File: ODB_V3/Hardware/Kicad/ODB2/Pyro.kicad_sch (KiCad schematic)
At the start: 51 parts, among them J1 Screw_Terminal_01x08, U11 SI5442DU-T1-GE3, U12 SI5442DU-T1-GE3, U2 LM339, U3 SI5442DU-T1-GE3, U8 SI5442DU-T1-GE3

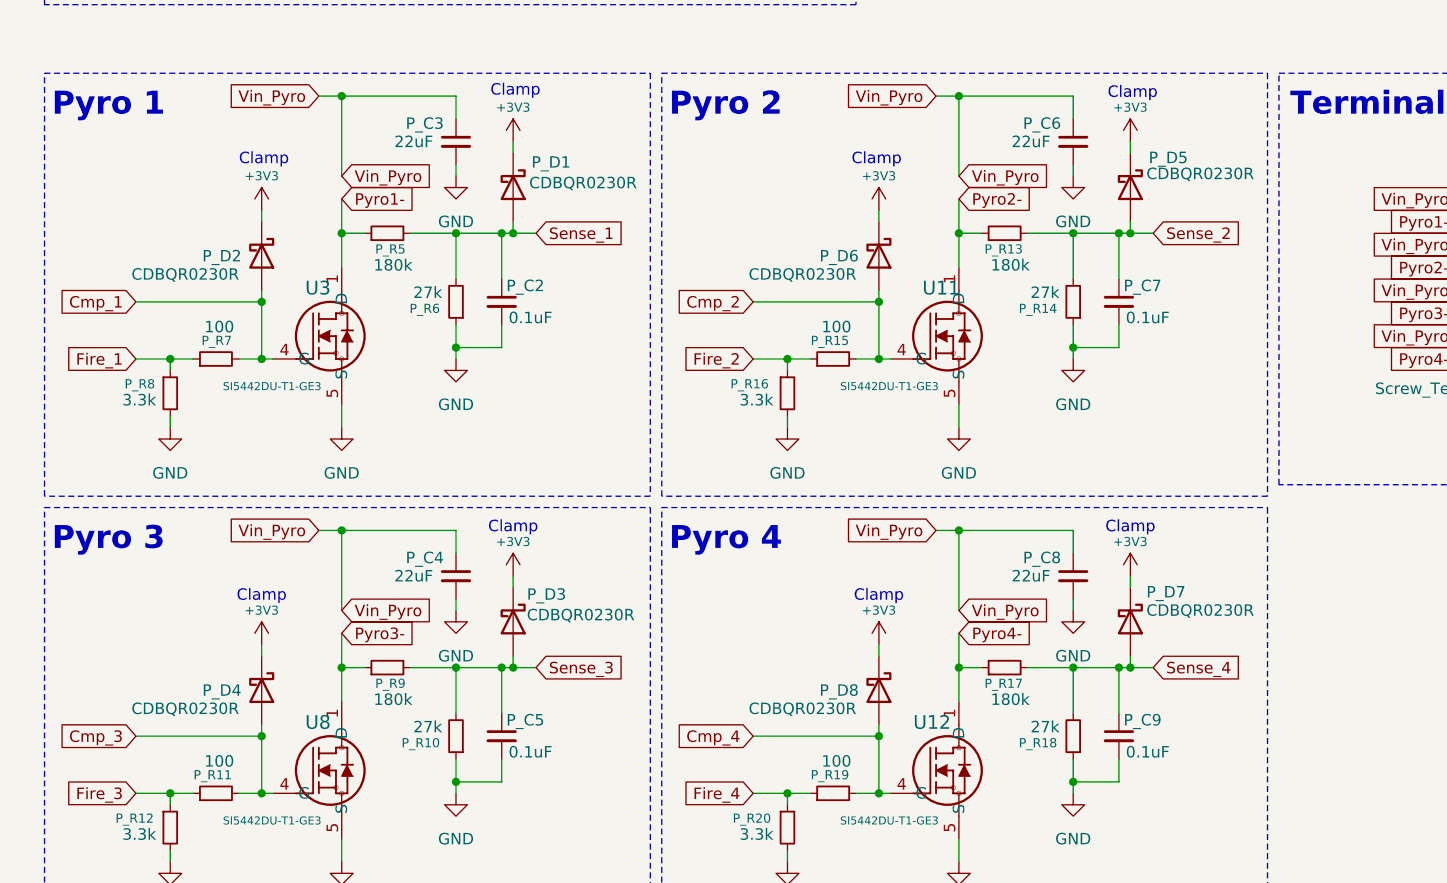
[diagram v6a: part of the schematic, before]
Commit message: wip : digikey part number et lien pour toutes pièces importantes (pas résistances, capacités, etc)
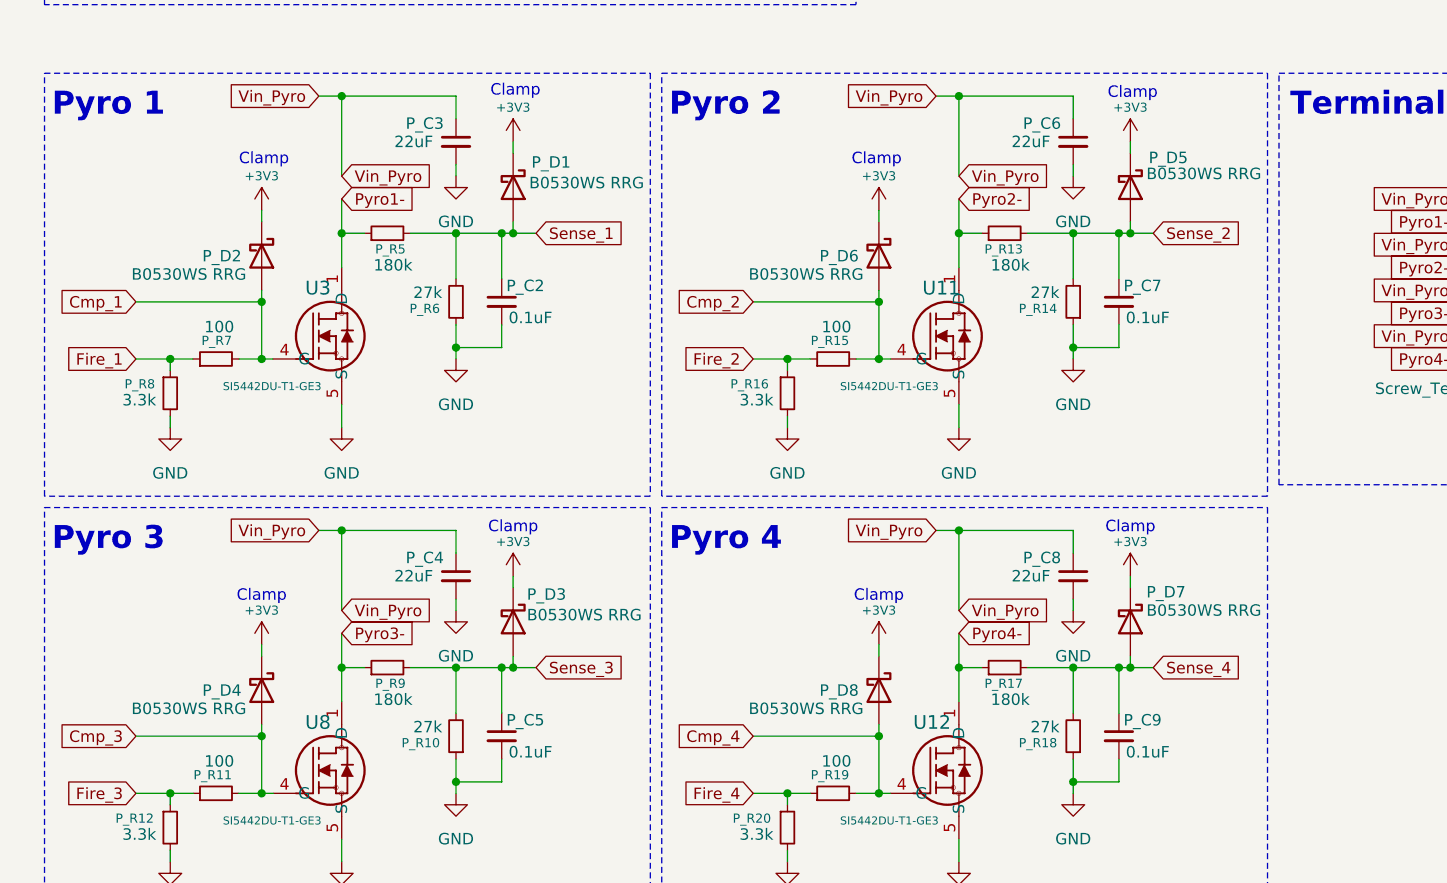
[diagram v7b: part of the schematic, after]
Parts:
- J1: DigiKey_Part_Number (none) -> 277-1279-ND
- PA_Q1: DigiKey_Part_Number (none) -> MMBT3904LT1GOSCT-ND; Digikey (none) -> MMBT3904LT1GOSCT-ND
- PA_Q3: DigiKey_Part_Number (none) -> SI7617DN-T1-GE3CT-ND
- P_D1, P_D2, P_D3, P_D4, P_D5, P_D6, P_D7, P_D8: value CDBQR0230R -> B0530WS RRG; DigiKey_Part_Number (none) -> B0530WSRRGCT-ND
- U11, U12, U3, U8: DigiKey_Part_Number (none) -> SI5442DU-T1-GE3CT-ND
- U2: DigiKey_Part_Number (none) -> 296-1013-1-ND; Purchase-URL (none) -> https://www.digikey.ca/en/products/detail/texas-instruments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
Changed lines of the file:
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@@
 			)
 		)
-		(property "Datasheet" "https://www.vishay.com/doc?63233"
+		(property "Datasheet" "https://www.digikey.com/en/products/detail/vishay-siliconix/SI5442DU-T1-GE3/4142130"
 			(at 109.22 177.8 0)
 			(effects
@@
 			)
 		)
-		(property "DigiKey_Part_Number" ""
+		(property "DigiKey_Part_Number" "SI5442DU-T1-GE3CT-ND"
 			(at 109.22 177.8 0)
 			(effects
@@
 			)
 		)
-		(property "Value" "CDBQR0230R"
+		(property "Value" "B0530WS RRG"
 			(at 69.088 109.982 90)
 			(effects
@@
 			)
 		)
-		(property "Datasheet" "https://assets.nexperia.com/documents/data-sheet/BAT54J.pdf"
+		(property "Datasheet" "https://www.digikey.ca/en/products/detail/taiwan-semiconductor-corporation/B0530WS-RRG/7357154"
 			(at 67.31 110.49 0)
 			(effects
@@
 			)
 		)
-		(property "DigiKey_Part_Number" ""
+		(property "DigiKey_Part_Number" "B0530WSRRGCT-ND"
 			(at 67.31 110.49 90)
 			(effects
@@
 			)
 		)
-		(property "DigiKey_Part_Number" ""
+		(property "DigiKey_Part_Number" "296-1013-1-ND"
 			(at 58.42 46.99 0)
 			(effects
@@
 			)
 		)
-		(property "Purchase-URL" ""
+		(property "Purchase-URL" "https://www.digikey.ca/en/products/detail/texas-instruments/LM339DR/276657"
 			(at 58.42 46.99 0)
 			(effects
@@
 			)
 		)
-		(property "Value" "CDBQR0230R"
+		(property "Value" "B0530WS RRG"
 			(at 68.834 157.988 90)
 			(effects
@@
 			)
 		)
-		(property "Datasheet" "https://assets.nexperia.com/documents/data-sheet/BAT54J.pdf"
+		(property "Datasheet" "https://www.digikey.ca/en/products/detail/taiwan-semiconductor-corporation/B0530WS-RRG/7357154"
 			(at 67.31 158.75 0)
 			(effects
@@
 			)
 		)
-		(property "DigiKey_Part_Number" ""
+		(property "DigiKey_Part_Number" "B0530WSRRGCT-ND"
 			(at 67.31 158.75 90)
 			(effects
@@
 			)
 		)
-		(property "DigiKey_Part_Number" ""
+		(property "DigiKey_Part_Number" "296-1013-1-ND"
 			(at 58.42 72.39 0)
 			(effects
@@
 			)
 		)
-		(property "Purchase-URL" ""
+		(property "Purchase-URL" "https://www.digikey.ca/en/products/detail/texas-instruments/LM339DR/276657"
 			(at 58.42 72.39 0)
 			(effects
@@
 			)
 		)
-		(property "Value" "CDBQR0230R"
+		(property "Value" "B0530WS RRG"
 			(at 24.892 120.142 90)
 			(effects
@@
 			)
 		)
-		(property "Datasheet" "https://assets.nexperia.com/documents/data-sheet/BAT54J.pdf"
+		(property "Datasheet" "https://www.digikey.ca/en/products/detail/taiwan-semiconductor-corporation/B0530WS-RRG/7357154"
 			(at 39.37 118.11 0)
 			(effects
@@
 			)
 		)
-		(property "DigiKey_Part_Number" ""
+		(property "DigiKey_Part_Number" "B0530WSRRGCT-ND"
 			(at 39.37 118.11 90)
 			(effects
@@
 			)
 		)
-		(property "Value" "CDBQR0230R"
+		(property "Value" "B0530WS RRG"
 			(at 24.892 168.402 90)
 			(effects
@@
 			)
 		)
-		(property "Datasheet" "https://assets.nexperia.com/documents/data-sheet/BAT54J.pdf"
+		(property "Datasheet" "https://www.digikey.ca/en/products/detail/taiwan-semiconductor-corporation/B0530WS-RRG/7357154"
 			(at 39.37 166.37 0)
 			(effects
@@
 			)
 		)
-		(property "DigiKey_Part_Number" ""
+		(property "DigiKey_Part_Number" "B0530WSRRGCT-ND"
 			(at 39.37 166.37 90)
 			(effects
@@
 			)
 		)
-		(property "DigiKey_Part_Number" ""
+		(property "DigiKey_Part_Number" "296-1013-1-ND"
 			(at 58.42 34.29 0)
 			(effects
@@
 			)
 		)
-		(property "Purchase-URL" ""
+		(property "Purchase-URL" "https://www.digikey.ca/en/products/detail/texas-instruments/LM339DR/276657"
 			(at 58.42 34.29 0)
 			(effects
@@
 			)
 		)
-		(property "Datasheet" "https://www.onsemi.com/pdf/datasheet/pzt3904-d.pdf"
+		(property "Datasheet" "https://www.digikey.ca/en/products/detail/onsemi/MMBT3904LT1G/1139813"
 			(at 215.9 49.53 0)
 			(effects
@@
 			)
 		)
-		(property "DigiKey_Part_Number" ""
+		(property "DigiKey_Part_Number" "MMBT3904LT1GOSCT-ND"
 			(at 215.9 49.53 0)
 			(effects
@@
 			)
 		)
+		(property "Digikey" "MMBT3904LT1GOSCT-ND"
+			(at 215.9 49.53 0)
+			(effects
+				(font
+					(size 1.27 1.27)
+				)
+				(hide yes)
+			)
+		)
 		(pin "1"
 		)
@@
 			)
 		)
-		(property "Datasheet" "https://www.vishay.com/doc?63233"
+		(property "Datasheet" "https://www.digikey.com/en/products/detail/vishay-siliconix/SI5442DU-T1-GE3/4142130"
 			(at 109.22 129.54 0)
 			(effects
@@
 			)
 		)
-		(property "DigiKey_Part_Number" ""
+		(property "DigiKey_Part_Number" "SI5442DU-T1-GE3CT-ND"
 			(at 109.22 129.54 0)
 			(effects
@@
 			)
 		)
-		(property "Datasheet" "https://www.vishay.com/doc?65164"
+		(property "Datasheet" "https://www.digikey.ca/en/products/detail/vishay-siliconix/SI7617DN-T1-GE3/2441735"
 			(at 226.06 33.02 0)
 			(effects
@@
 			)
 		)
-		(property "DigiKey_Part_Number" ""
+		(property "DigiKey_Part_Number" "SI7617DN-T1-GE3CT-ND"
 			(at 226.06 33.02 0)
 			(effects
@@
 			)
 		)
-		(property "DigiKey_Part_Number" ""
+		(property "DigiKey_Part_Number" "296-1013-1-ND"
 			(at 90.17 53.34 0)
 			(effects
@@
 			)
 		)
-		(property "Purchase-URL" ""
+		(property "Purchase-URL" "https://www.digikey.ca/en/products/detail/texas-instruments/LM339DR/276657"
 			(at 90.17 53.34 0)
 			(effects
@@
 			)
 		)
-		(property "Datasheet" "~"
+		(property "Datasheet" "https://www.digikey.ca/en/products/detail/phoenix-contact/1725711/267468?gclsrc=aw.ds&gad_source=1&gad_campaignid=20539025167&gbraid=0AAAAADrbLli7yMF8AWC3OGDeDtnxtbfT4&gclid=CjwKCAiAmePKBhAfEiwAU3Ko3HDFvolF9BsdpkRYg5j-UTxoh0sbjQ5grqNJHSHlJ0Sb2VUXdgPsrBoCaTUQAvD_BwE"
 			(at 181.61 119.38 0)
 			(effects
@@
 			)
 		)
-		(property "DigiKey_Part_Number" ""
+		(property "DigiKey_Part_Number" "277-1279-ND"
 			(at 181.61 119.38 0)
 			(effects
@@
 			)
 		)
-		(property "Datasheet" "https://www.vishay.com/doc?63233"
+		(property "Datasheet" "https://www.digikey.com/en/products/detail/vishay-siliconix/SI5442DU-T1-GE3/4142130"
 			(at 40.64 177.8 0)
 			(effects
@@
 			)
 		)
-		(property "DigiKey_Part_Number" ""
+		(property "DigiKey_Part_Number" "SI5442DU-T1-GE3CT-ND"
 			(at 40.64 177.8 0)
 			(effects
@@
 			)
 		)
-		(property "Datasheet" "https://www.vishay.com/doc?63233"
+		(property "Datasheet" "https://www.digikey.com/en/products/detail/vishay-siliconix/SI5442DU-T1-GE3/4142130"
 			(at 40.64 129.54 0)
 			(effects
@@
 			)
 		)
-		(property "DigiKey_Part_Number" ""
+		(property "DigiKey_Part_Number" "SI5442DU-T1-GE3CT-ND"
 			(at 40.64 129.54 0)
 			(effects
@@
 			)
 		)
-		(property "DigiKey_Part_Number" ""
+		(property "DigiKey_Part_Number" "296-1013-1-ND"
 			(at 58.42 59.69 0)
 			(effects
@@
 			)
 		)
-		(property "Purchase-URL" ""
+		(property "Purchase-URL" "https://www.digikey.ca/en/products/detail/texas-instruments/LM339DR/276657"
 			(at 58.42 59.69 0)
 			(effects
@@
 			)
 		)
-		(property "Value" "CDBQR0230R"
+		(property "Value" "B0530WS RRG"
 			(at 93.472 120.142 90)
 			(effects
@@
 			)
 		)
-		(property "Datasheet" "https://assets.nexperia.com/documents/data-sheet/BAT54J.pdf"
+		(property "Datasheet" "https://www.digikey.ca/en/products/detail/taiwan-semiconductor-corporation/B0530WS-RRG/7357154"
 			(at 107.95 118.11 0)
 			(effects
@@
 			)
 		)
-		(property "DigiKey_Part_Number" ""
+		(property "DigiKey_Part_Number" "B0530WSRRGCT-ND"
 			(at 107.95 118.11 90)
 			(effects
@@
 			)
 		)
-		(property "Value" "CDBQR0230R"
+		(property "Value" "B0530WS RRG"
 			(at 137.668 157.48 90)
 			(effects
@@
 			)
 		)
-		(property "Datasheet" "https://assets.nexperia.com/documents/data-sheet/BAT54J.pdf"
+		(property "Datasheet" "https://www.digikey.ca/en/products/detail/taiwan-semiconductor-corporation/B0530WS-RRG/7357154"
 			(at 135.89 158.75 0)
 			(effects
@@
 			)
 		)
-		(property "DigiKey_Part_Number" ""
+		(property "DigiKey_Part_Number" "B0530WSRRGCT-ND"
 			(at 135.89 158.75 90)
 			(effects
@@
 			)
 		)
-		(property "Value" "CDBQR0230R"
+		(property "Value" "B0530WS RRG"
 			(at 137.668 108.966 90)
 			(effects
@@
 			)
 		)
-		(property "Datasheet" "https://assets.nexperia.com/documents/data-sheet/BAT54J.pdf"
+		(property "Datasheet" "https://www.digikey.ca/en/products/detail/taiwan-semiconductor-corporation/B0530WS-RRG/7357154"
 			(at 135.89 110.49 0)
 			(effects
@@
 			)
 		)
-		(property "DigiKey_Part_Number" ""
+		(property "DigiKey_Part_Number" "B0530WSRRGCT-ND"
 			(at 135.89 110.49 90)
 			(effects
@@
 			)
 		)
-		(property "Value" "CDBQR0230R"
+		(property "Value" "B0530WS RRG"
 			(at 93.472 168.402 90)
 			(effects
@@
 			)
 		)
-		(property "Datasheet" "https://assets.nexperia.com/documents/data-sheet/BAT54J.pdf"
+		(property "Datasheet" "https://www.digikey.ca/en/products/detail/taiwan-semiconductor-corporation/B0530WS-RRG/7357154"
 			(at 107.95 166.37 0)
 			(effects
@@
 			)
 		)
-		(property "DigiKey_Part_Number" ""
+		(property "DigiKey_Part_Number" "B0530WSRRGCT-ND"
 			(at 107.95 166.37 90)
 			(effects

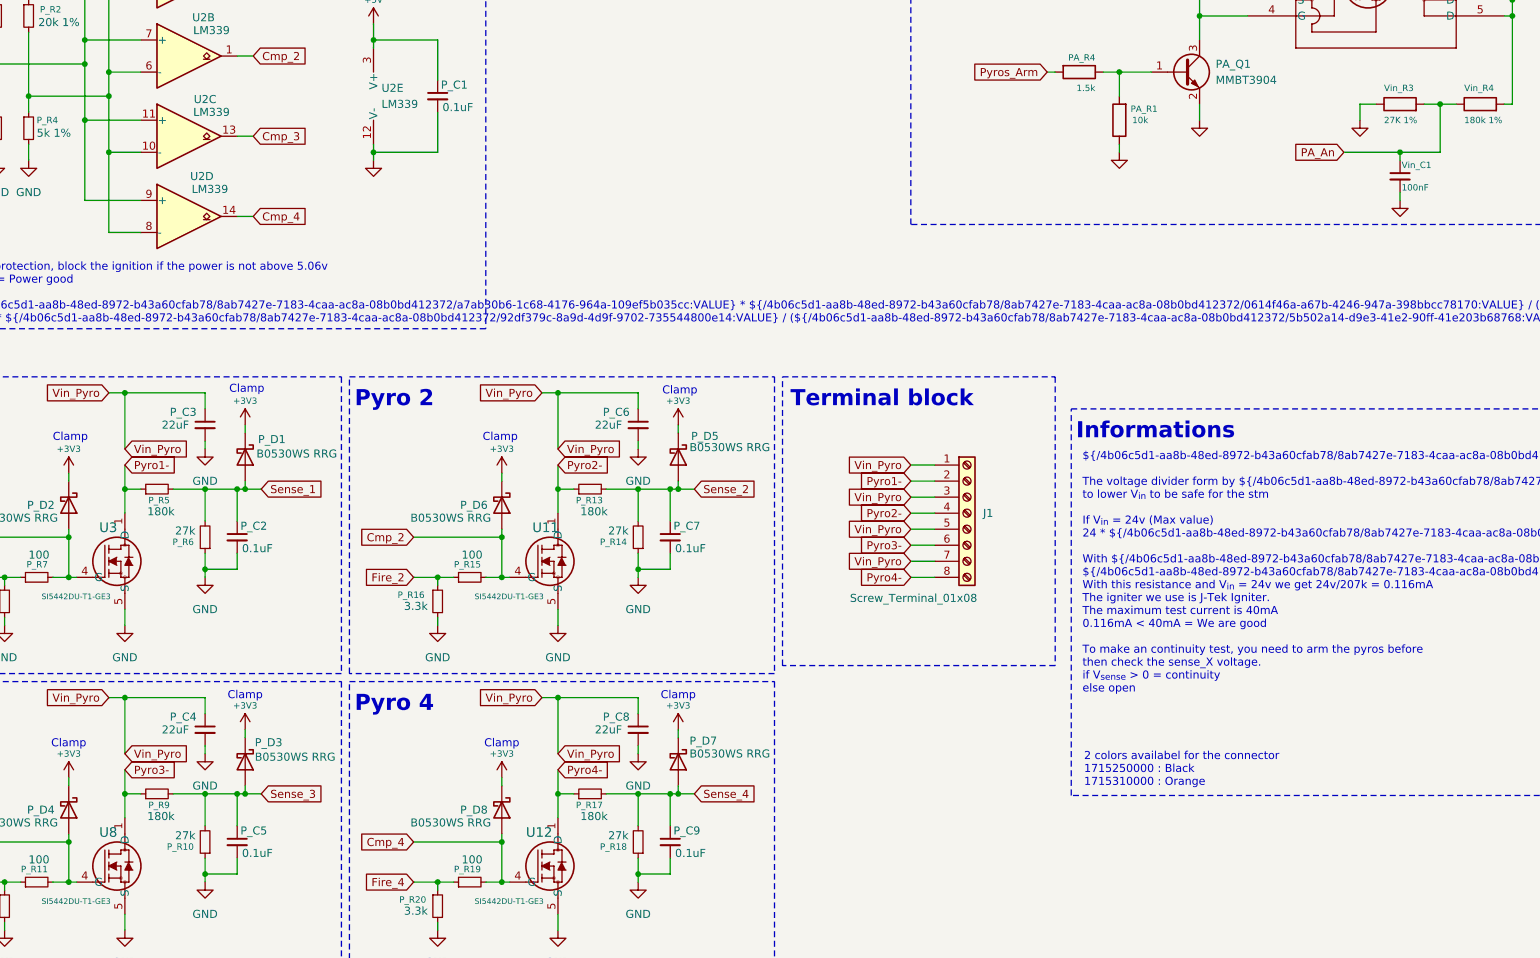
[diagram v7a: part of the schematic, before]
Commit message: fix : change pieces and footprints to reduce BOM
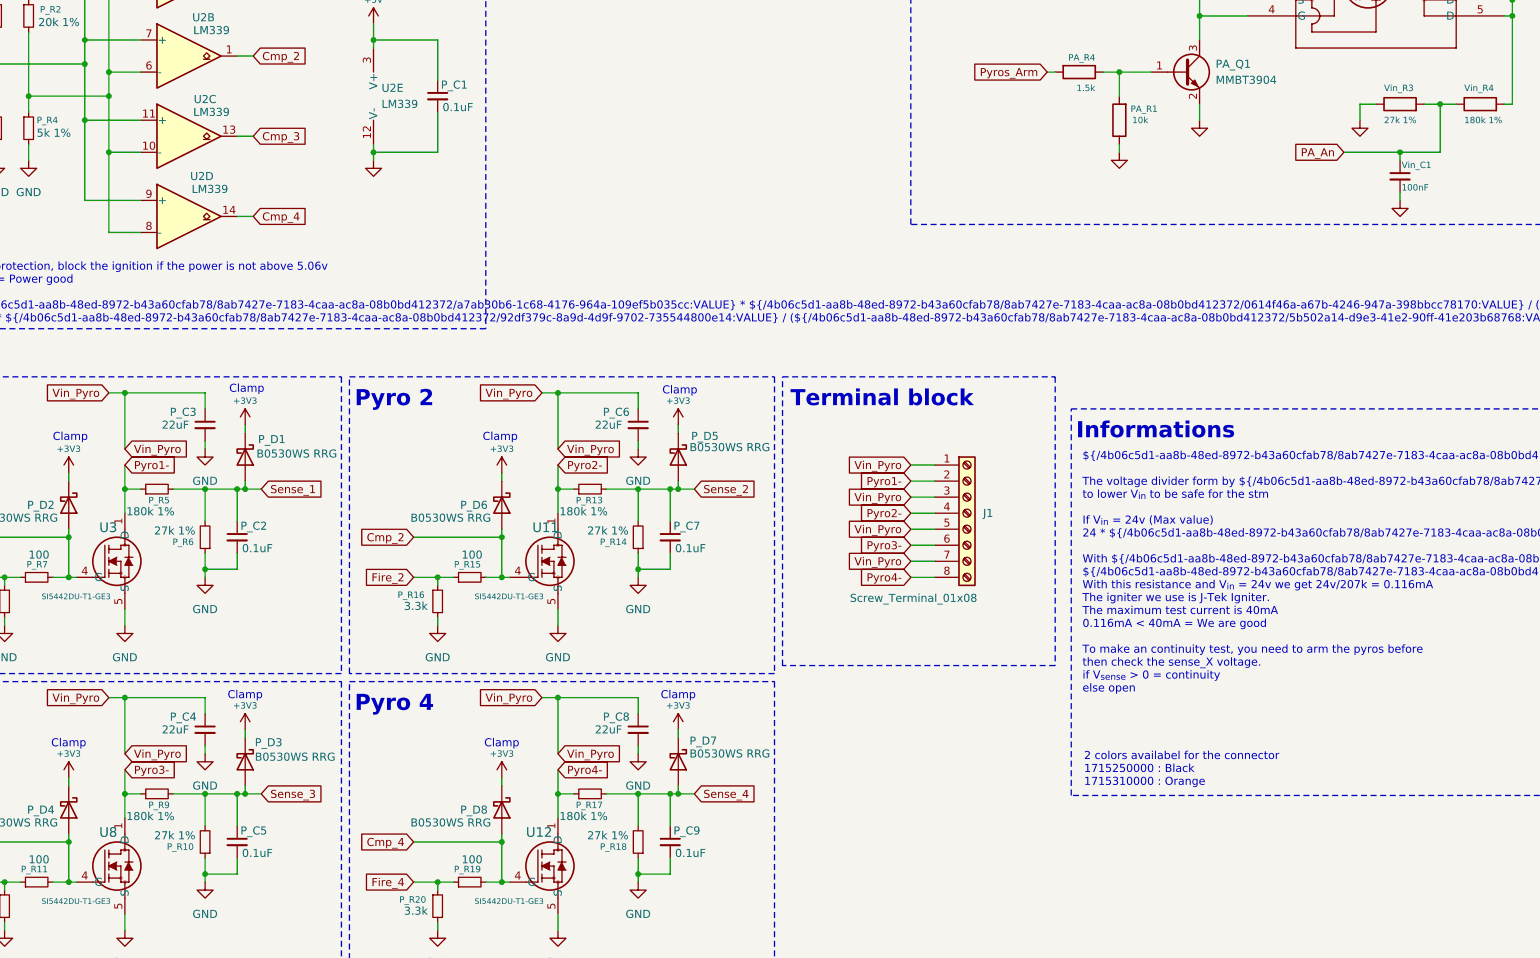
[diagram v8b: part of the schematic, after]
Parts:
- P_R10, P_R14, P_R18, P_R6: value 27k -> 27k 1%
- P_R13, P_R17, P_R5, P_R9: value 180k -> 180k 1%
- Vin_R3: value 27K 1% -> 27k 1%
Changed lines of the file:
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@@
 			)
 		)
-		(property "Value" "27k"
+		(property "Value" "27k 1%"
 			(at 128.016 170.434 0)
 			(effects
@@
 			)
 		)
-		(property "Value" "180k"
+		(property "Value" "180k 1%"
 			(at 56.134 119.126 90)
 			(effects
@@
 			)
 		)
-		(property "Value" "27K 1%"
+		(property "Value" "27k 1%"
 			(at 247.65 57.15 90)
 			(effects
@@
 			)
 		)
-		(property "Value" "27k"
+		(property "Value" "27k 1%"
 			(at 59.436 122.174 0)
 			(effects
@@
 			)
 		)
-		(property "Value" "180k"
+		(property "Value" "180k 1%"
 			(at 124.714 167.386 90)
 			(effects
@@
 			)
 		)
-		(property "Value" "180k"
+		(property "Value" "180k 1%"
 			(at 124.714 119.126 90)
 			(effects
@@
 			)
 		)
-		(property "Value" "27k"
+		(property "Value" "27k 1%"
 			(at 128.016 122.174 0)
 			(effects
@@
 			)
 		)
-		(property "Value" "180k"
+		(property "Value" "180k 1%"
 			(at 56.134 167.386 90)
 			(effects
@@
 			)
 		)
-		(property "Value" "27k"
+		(property "Value" "27k 1%"
 			(at 59.436 170.434 0)
 			(effects
